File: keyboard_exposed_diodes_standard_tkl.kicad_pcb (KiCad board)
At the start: 2 copper layers, 362 x 177 mm, 317 parts, among them J1 Conn_01x02_Male, J2 USB_C_Receptacle_USB2.0, SW1 Rotary_Encoder_Switch, U1 Pico

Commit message: Adding Net Names
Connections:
- net Net-(C1-Pad1) renamed PWR
- net Net-(C1-Pad2) renamed GND
- net Net-(D_0-Pad1) renamed ROW 1
- net Net-(D_A1-Pad1) renamed ROW 3
- net Net-(D_B1-Pad1) renamed ROW 4
- net Net-(D_BSLASH1-Pad1) renamed ROW 2
- net Net-(D_DOWN1-Pad1) renamed ROW 5
- net Net-(D_ESC1-Pad1) renamed ROW 0
- net Net-(SW1-PadS2) renamed COL 1
- net Net-(U1-Pad1) renamed COL 0
- net Net-(U1-Pad10) renamed COL 7
- net Net-(U1-Pad11) renamed COL 8
- net Net-(U1-Pad12) renamed COL 9
- net Net-(U1-Pad14) renamed COL 10
- net Net-(U1-Pad15) renamed COL 11
- net Net-(U1-Pad16) renamed COL 12
- net Net-(U1-Pad17) renamed COL 13
- net Net-(U1-Pad19) renamed COL 14
- net Net-(U1-Pad20) renamed COL 15
- net Net-(U1-Pad21) renamed COL 16
- net Net-(U1-Pad4) renamed COL 2
- net Net-(U1-Pad5) renamed COL 3
- net Net-(U1-Pad6) renamed COL 4
- net Net-(U1-Pad7) renamed COL 5
- net Net-(U1-Pad9) renamed COL 6

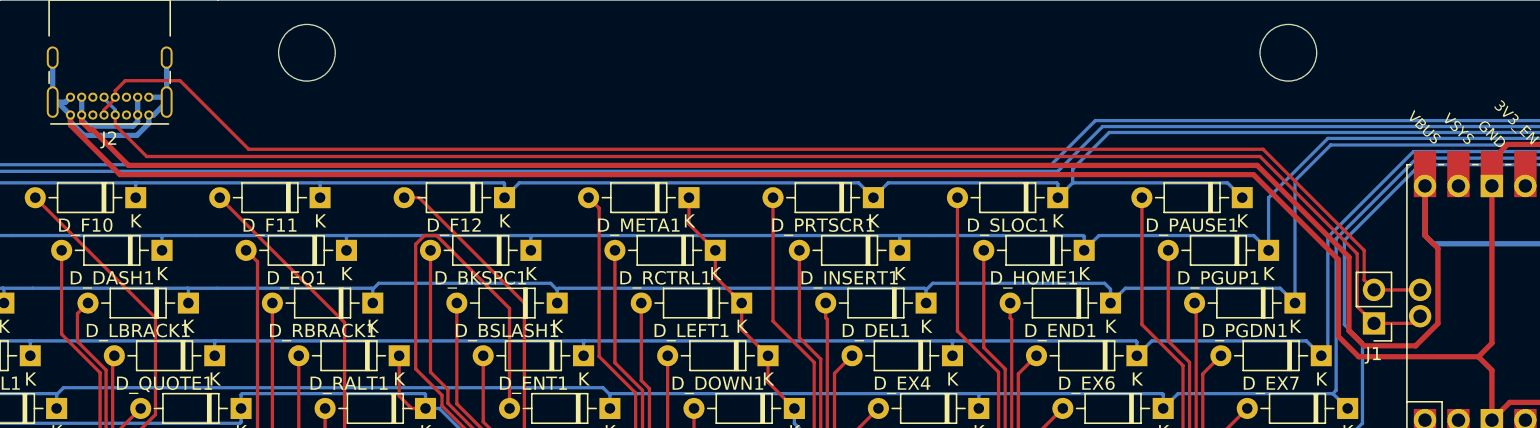
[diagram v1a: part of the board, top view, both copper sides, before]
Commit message: REduce PCB Spacing to match jlcpcb minimum. Redo USB C data traces
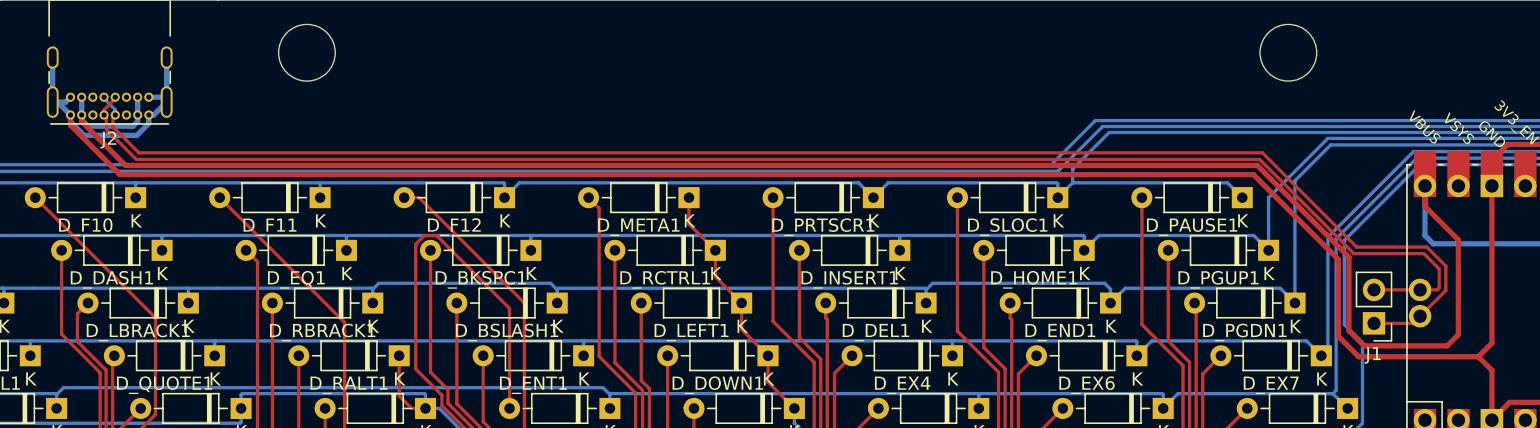
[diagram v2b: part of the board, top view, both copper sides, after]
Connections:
- net Net-(J1-Pad1) renamed /D+
- net Net-(J1-Pad2) renamed /D-
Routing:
- net /D+: track 110.3 -> 116.6 mm
- net /D-: track 109.5 -> 114.9 mm
- net PWR: track 2854.3 -> 2857.0 mm
